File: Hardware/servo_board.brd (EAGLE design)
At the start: 30.5 x 50.8 mm, 33 parts, among them U1 PCA9685, U2 PCA9306

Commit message: Add version info
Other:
- board text added: "v01"
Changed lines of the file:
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@@
 <dimension x1="29.28210625" y1="41.83789375" x2="27.86789375" y2="43.25210625" x3="34.29" y3="48.26" textsize="1.778" layer="51" dtype="diameter"/>
 <text x="29.21" y="6.35" size="1.016" layer="22" font="vector" ratio="15" rot="MR90" align="center">4xM2.0</text>
+<text x="1.27" y="3.81" size="1.778" layer="1" font="vector" ratio="15">v01</text>
 </plain>
 <attributes>
@@
 <wire x1="3.048" y1="40.005" x2="1.905" y2="40.005" width="0.254" layer="16"/>
 <via x="16.51" y="13.97" extent="1-16" drill="0.508"/>
-<wire x1="27.1272" y1="20.5232" x2="28.2448" y2="22.1742" width="0" layer="19" extent="1-1"/>
-<wire x1="25.96" y1="20.58" x2="27.1272" y2="20.5232" width="0" layer="19" extent="16-16"/>
-<wire x1="25.96" y1="20.5798" x2="25.96" y2="20.58" width="0" layer="19" extent="1-16"/>
-<wire x1="25.96" y1="20.98" x2="25.96" y2="20.58" width="0" layer="19" extent="16-16"/>
-<wire x1="25.96" y1="20.9798" x2="25.96" y2="20.98" width="0" layer="19" extent="1-16"/>
-<wire x1="25.96" y1="21.38" x2="25.96" y2="20.98" width="0" layer="19" extent="16-16"/>
-<wire x1="25.96" y1="21.3798" x2="25.96" y2="21.38" width="0" layer="19" extent="1-16"/>
-<wire x1="25.96" y1="20.18" x2="25.96" y2="20.58" width="0" layer="19" extent="16-16"/>
-<wire x1="25.96" y1="20.1798" x2="25.96" y2="20.18" width="0" layer="19" extent="1-16"/>
-<wire x1="25.96" y1="22.18" x2="25.96" y2="21.38" width="0" layer="19" extent="16-16"/>
-<wire x1="25.96" y1="22.1798" x2="25.96" y2="22.18" width="0" layer="19" extent="1-16"/>
-<wire x1="25.96" y1="22.98" x2="25.96" y2="22.18" width="0" layer="19" extent="16-16"/>
-<wire x1="25.96" y1="22.9798" x2="25.96" y2="22.98" width="0" layer="19" extent="1-16"/>
-<wire x1="17.145" y1="26.25" x2="25.96" y2="22.98" width="0" layer="19" extent="1-16"/>
-<wire x1="13.705" y1="28.6" x2="17.145" y2="26.25" width="0" layer="19" extent="1-1"/>
-<wire x1="13.055" y1="28.6" x2="13.705" y2="28.6" width="0" layer="19" extent="1-1"/>
-<wire x1="13.705" y1="22.2" x2="17.145" y2="26.25" width="0" layer="19" extent="1-1"/>
-<wire x1="13.055" y1="22.2" x2="13.705" y2="22.2" width="0" layer="19" extent="1-1"/>
-<wire x1="12.405" y1="22.2" x2="13.055" y2="22.2" width="0" layer="19" extent="1-1"/>
-<wire x1="7.205" y1="28.6" x2="13.055" y2="28.6" width="0" layer="19" extent="1-1"/>
-<wire x1="8.04" y1="15.24" x2="12.405" y2="22.2" width="0" layer="19" extent="1-1"/>
-<wire x1="10.199" y1="11.43" x2="8.04" y2="15.24" width="0" layer="19" extent="1-1"/>
-<wire x1="14.74" y1="12.5238" x2="10.199" y2="11.43" width="0" layer="19" extent="1-1"/>
-<wire x1="16.51" y1="13.97" x2="14.74" y2="12.5238" width="0" layer="19" extent="1-1"/>
-<wire x1="3.048" y1="40.005" x2="7.205" y2="28.6" width="0" layer="19" extent="1-16"/>
 </signal>
 <signal name="VSYS">

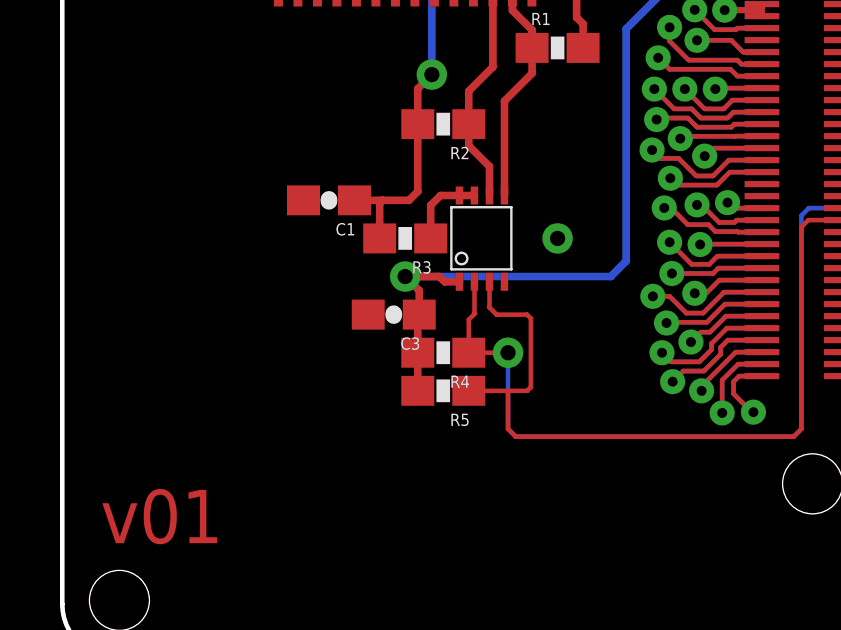
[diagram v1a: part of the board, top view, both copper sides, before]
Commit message: Touch up silk, resistor placement
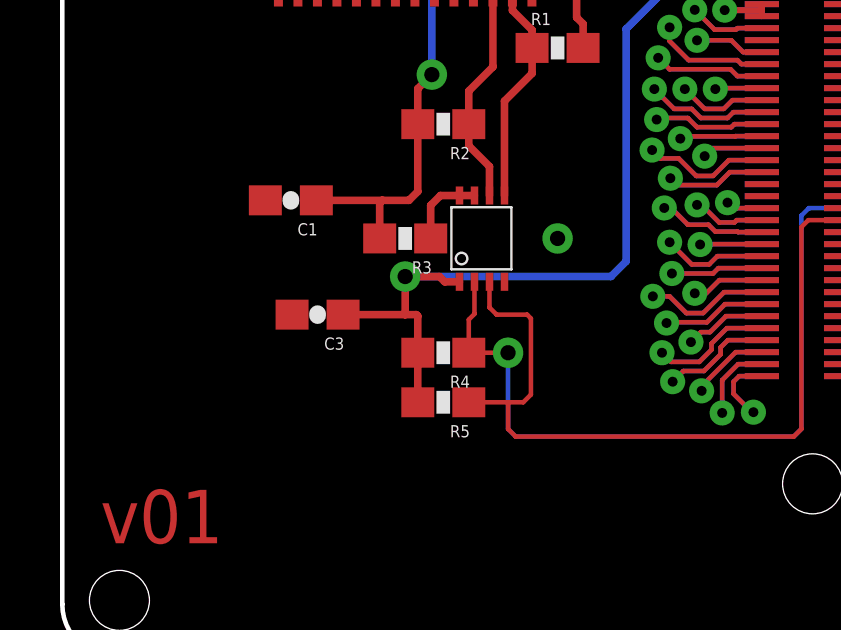
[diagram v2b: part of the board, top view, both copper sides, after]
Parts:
- moved C3 2.54 mm to (8.51, 11.4)
- moved C1 1.27 mm to (7.62, 15.2)
- moved R5 0.38 mm to (12.7, 8.51)
- renumbered U$2 to U3, U$3 to U4
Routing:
- net 1.8V: track 29.4 -> 32.0 mm
- net VSYS: track 32.5 -> 33.7 mm
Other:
- board text added: "8-Servo Controller"
- board text added: "GND"
- board text added: "M Hord"
- board text added: "SIG"
- board text added: "VIN"
- board text removed: "Casey Kuhns"
- board text removed: "Example Name of Board"

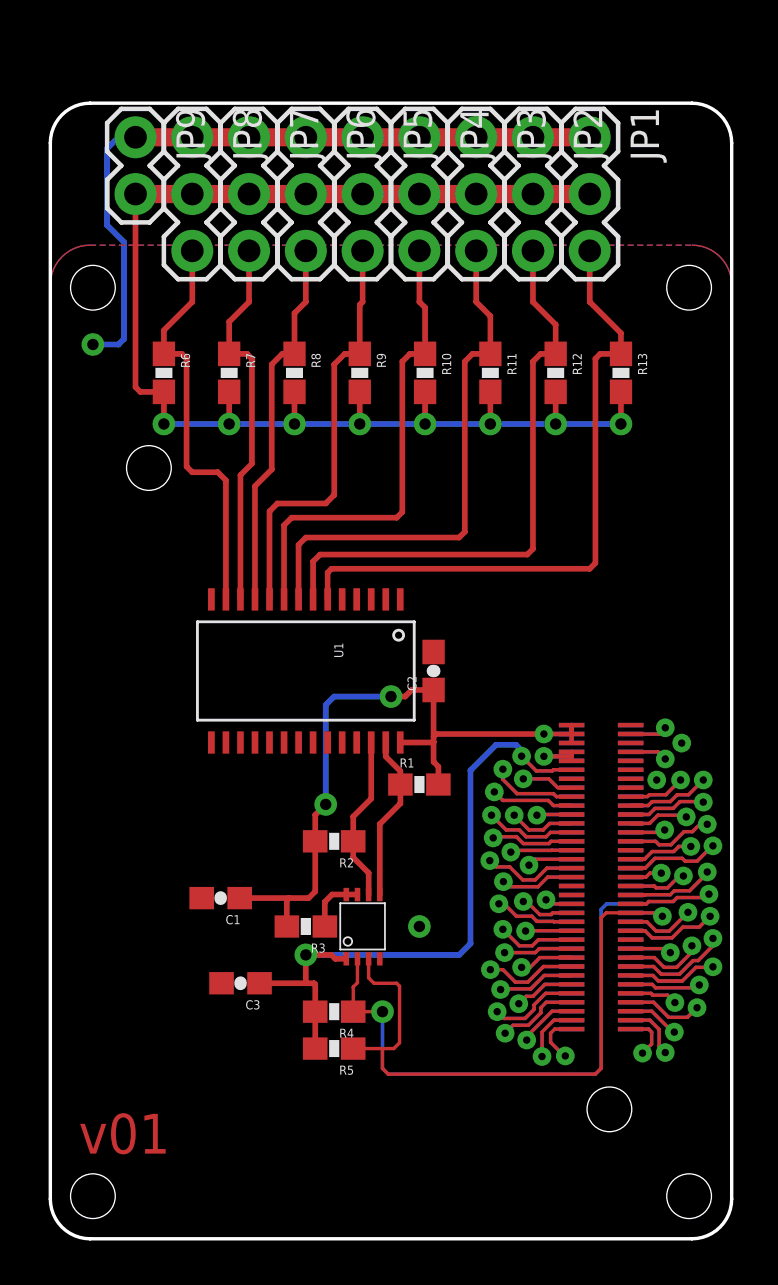
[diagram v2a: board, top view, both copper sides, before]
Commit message: Increased length of board by 100th
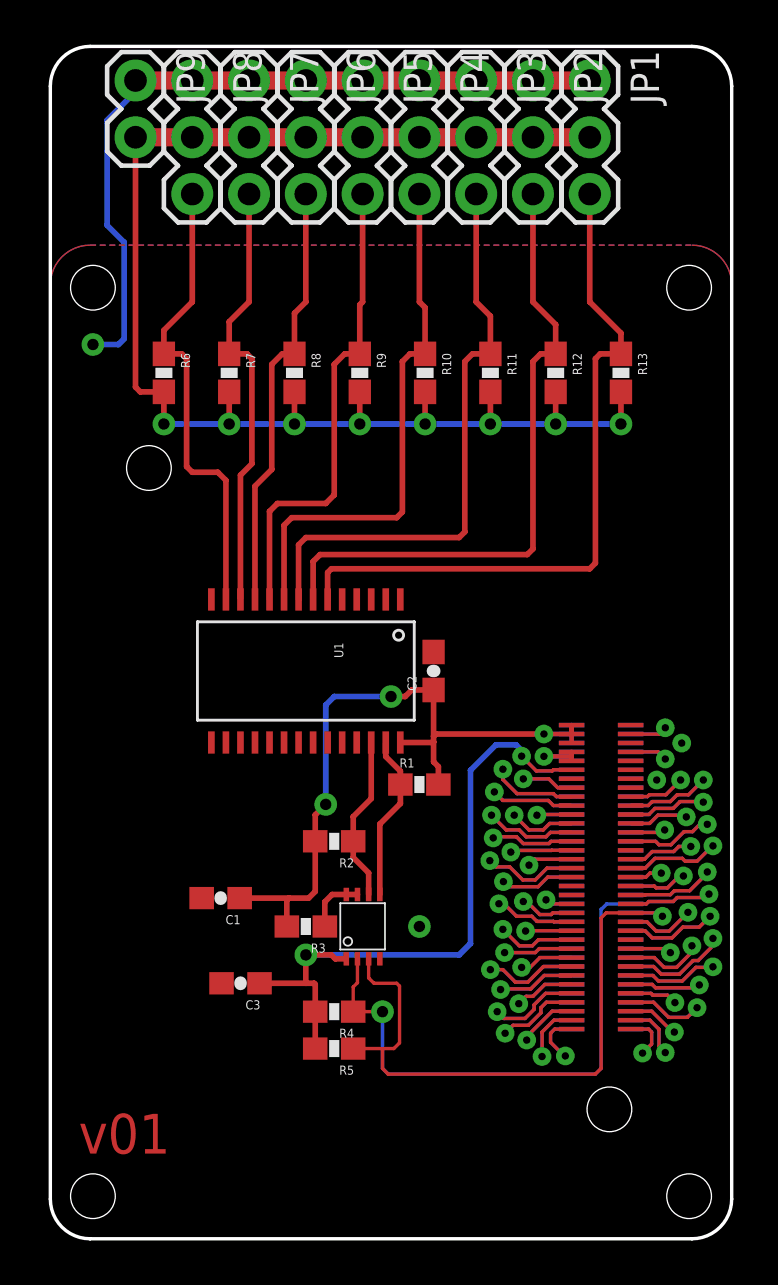
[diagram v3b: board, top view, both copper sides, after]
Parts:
- moved JP1 2.54 mm to (24.1, 51.8)
- moved JP2 2.54 mm to (21.6, 51.8)
- moved JP3 2.54 mm to (19.1, 51.8)
- moved JP4 2.54 mm to (16.5, 51.8)
- moved JP5 2.54 mm to (14.0, 51.8)
- moved JP6 2.54 mm to (11.4, 51.8)
- moved JP7 2.54 mm to (8.89, 51.8)
- moved JP8 2.54 mm to (6.35, 51.8)
- moved JP9 2.54 mm to (3.81, 51.8)
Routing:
- net VCC: track 62.3 -> 64.8 mm
- net CH5: track 16.9 -> 19.4 mm
- net CH2: track 23.9 -> 26.4 mm
- net CH1: track 26.3 -> 28.9 mm
- net CH7: track 18.4 -> 21.0 mm
- net CH6: track 17.1 -> 19.6 mm
- net CH4: track 19.0 -> 21.5 mm
- net CH3: track 21.5 -> 24.0 mm
- net CH0: track 28.9 -> 31.5 mm
- net GND: track 32.1 -> 34.2 mm
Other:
- board size 30.5 x 50.8 mm -> 30.5 x 53.3 mm

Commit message: Skootch resistors out of keepout region.
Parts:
- moved R12 3.81 mm to (22.6, 42.5)
- moved R13 3.81 mm to (25.5, 42.5)
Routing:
- net VCC: track 64.8 -> 68.0 mm
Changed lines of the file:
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@@
 <attribute name="PROD_ID" value="RES-07856" x="0.635" y="56.515" size="1.778" layer="27" font="vector" ratio="15" rot="R270" display="off"/>
 </element>
-<element name="R12" library="SparkFun-Resistors" package="0603-RES" value="1K" x="22.606" y="38.735" rot="R270">
-<attribute name="PROD_ID" value="RES-07856" x="-0.254" y="60.325" size="1.778" layer="27" font="vector" ratio="15" rot="R270" display="off"/>
+<element name="R12" library="SparkFun-Resistors" package="0603-RES" value="1K" x="22.606" y="42.545" rot="R270">
+<attribute name="PROD_ID" value="RES-07856" x="-0.254" y="64.135" size="1.778" layer="27" font="vector" ratio="15" rot="R270" display="off"/>
 </element>
-<element name="R13" library="SparkFun-Resistors" package="0603-RES" value="1K" x="25.527" y="38.735" rot="R270">
-<attribute name="PROD_ID" value="RES-07856" x="-1.143" y="64.135" size="1.778" layer="27" font="vector" ratio="15" rot="R270" display="off"/>
+<element name="R13" library="SparkFun-Resistors" package="0603-RES" value="1K" x="25.527" y="42.545" rot="R270">
+<attribute name="PROD_ID" value="RES-07856" x="-1.143" y="67.945" size="1.778" layer="27" font="vector" ratio="15" rot="R270" display="off"/>
 </element>
 <element name="JP1" library="SparkFun-Connectors" package="1X03" value="" x="24.13" y="51.816" rot="R270"/>
@@
 <contactref element="U1" pad="6"/>
 <contactref element="JP1" pad="3"/>
-<wire x1="25.527" y1="39.585" x2="25.527" y2="40.513" width="0.254" layer="1"/>
-<wire x1="25.527" y1="40.513" x2="24.13" y2="41.91" width="0.254" layer="1"/>
-<wire x1="24.13" y1="41.91" x2="24.13" y2="46.736" width="0.254" layer="1"/>
+<wire x1="25.527" y1="43.395" x2="25.527" y2="44.323" width="0.254" layer="1"/>
+<wire x1="25.527" y1="44.323" x2="24.13" y2="45.72" width="0.254" layer="1"/>
+<wire x1="24.13" y1="45.72" x2="24.13" y2="46.736" width="0.254" layer="1"/>
 <wire x1="12.405" y1="28.6" x2="12.405" y2="29.804" width="0.254" layer="1"/>
 <wire x1="12.405" y1="29.804" x2="12.573" y2="29.972" width="0.254" layer="1"/>
-<wire x1="12.573" y1="29.972" x2="24.13" y2="29.972" width="0.254" layer="1"/>
-<wire x1="24.13" y1="29.972" x2="24.384" y2="30.226" width="0.254" layer="1"/>
-<wire x1="24.384" y1="30.226" x2="24.384" y2="39.37" width="0.254" layer="1"/>
-<wire x1="24.384" y1="39.37" x2="24.599" y2="39.585" width="0.254" layer="1"/>
-<wire x1="25.527" y1="39.585" x2="24.599" y2="39.585" width="0.254" layer="1"/>
+<wire x1="12.573" y1="29.972" x2="21.336" y2="29.972" width="0.254" layer="1"/>
+<wire x1="21.336" y1="29.972" x2="21.59" y2="30.226" width="0.254" layer="1"/>
+<wire x1="21.59" y1="30.226" x2="21.59" y2="39.37" width="0.254" layer="1"/>
+<wire x1="21.59" y1="39.37" x2="21.717" y2="39.497" width="0.254" layer="1"/>
+<wire x1="21.717" y1="39.497" x2="24.003" y2="39.497" width="0.254" layer="1"/>
+<wire x1="24.003" y1="39.497" x2="24.384" y2="39.878" width="0.254" layer="1"/>
+<wire x1="24.384" y1="39.878" x2="24.384" y2="43.18" width="0.254" layer="1"/>
+<wire x1="24.384" y1="43.18" x2="24.599" y2="43.395" width="0.254" layer="1"/>
+<wire x1="25.527" y1="43.395" x2="24.599" y2="43.395" width="0.254" layer="1"/>
 </signal>
 <signal name="CH1">
@@
 <contactref element="U1" pad="7"/>
 <contactref element="JP2" pad="3"/>
-<wire x1="22.606" y1="39.585" x2="22.606" y2="40.894" width="0.254" layer="1"/>
-<wire x1="22.606" y1="40.894" x2="21.59" y2="41.91" width="0.254" layer="1"/>
-<wire x1="21.59" y1="41.91" x2="21.59" y2="46.736" width="0.254" layer="1"/>
+<wire x1="22.606" y1="43.395" x2="22.606" y2="44.704" width="0.254" layer="1"/>
+<wire x1="22.606" y1="44.704" x2="21.59" y2="45.72" width="0.254" layer="1"/>
+<wire x1="21.59" y1="45.72" x2="21.59" y2="46.736" width="0.254" layer="1"/>
 <wire x1="11.755" y1="28.6" x2="11.755" y2="30.297" width="0.254" layer="1"/>
 <wire x1="11.755" y1="30.297" x2="12.065" y2="30.607" width="0.254" layer="1"/>
-<wire x1="12.065" y1="30.607" x2="21.336" y2="30.607" width="0.254" layer="1"/>
-<wire x1="21.336" y1="30.607" x2="21.59" y2="30.861" width="0.254" layer="1"/>
-<wire x1="21.59" y1="30.861" x2="21.59" y2="39.243" width="0.254" layer="1"/>
-<wire x1="22.606" y1="39.585" x2="21.932" y2="39.585" width="0.254" layer="1"/>
-<wire x1="21.932" y1="39.585" x2="21.59" y2="39.243" width="0.254" layer="1"/>
+<wire x1="12.065" y1="30.607" x2="20.32" y2="30.607" width="0.254" layer="1"/>
+<wire x1="20.32" y1="30.607" x2="20.701" y2="30.988" width="0.254" layer="1"/>
+<wire x1="20.701" y1="30.988" x2="20.701" y2="42.545" width="0.254" layer="1"/>
+<wire x1="22.606" y1="43.395" x2="21.551" y2="43.395" width="0.254" layer="1"/>
+<wire x1="21.551" y1="43.395" x2="20.701" y2="42.545" width="0.254" layer="1"/>
 </signal>
 <signal name="CH2">
@@
 <wire x1="19.685" y1="37.885" x2="19.685" y2="36.449" width="0.254" layer="1"/>
 <via x="19.685" y="36.449" extent="1-16" drill="0.508"/>
-<wire x1="22.606" y1="37.885" x2="22.606" y2="36.449" width="0.254" layer="1"/>
-<via x="22.606" y="36.449" extent="1-16" drill="0.508"/>
-<wire x1="25.527" y1="37.885" x2="25.527" y2="36.449" width="0.254" layer="1"/>
-<via x="25.527" y="36.449" extent="1-16" drill="0.508"/>
-<wire x1="25.527" y1="36.449" x2="22.606" y2="36.449" width="0.254" layer="16"/>
-<wire x1="19.685" y1="36.449" x2="22.606" y2="36.449" width="0.254" layer="16"/>
+<wire x1="22.606" y1="41.695" x2="22.606" y2="40.386" width="0.254" layer="1"/>
+<via x="22.606" y="40.386" extent="1-16" drill="0.508"/>
+<wire x1="25.527" y1="41.695" x2="25.527" y2="40.386" width="0.254" layer="1"/>
+<via x="25.527" y="40.386" extent="1-16" drill="0.508"/>
+<wire x1="25.527" y1="40.386" x2="22.606" y2="40.386" width="0.254" layer="16"/>
+<wire x1="19.685" y1="36.449" x2="20.574" y2="36.449" width="0.254" layer="16"/>
+<wire x1="20.574" y1="36.449" x2="20.955" y2="36.83" width="0.254" layer="16"/>
+<wire x1="20.955" y1="36.83" x2="20.955" y2="39.878" width="0.254" layer="16"/>
+<wire x1="20.955" y1="39.878" x2="21.463" y2="40.386" width="0.254" layer="16"/>
+<wire x1="21.463" y1="40.386" x2="22.606" y2="40.386" width="0.254" layer="16"/>
 <wire x1="19.685" y1="36.449" x2="16.764" y2="36.449" width="0.254" layer="16"/>
 <wire x1="16.764" y1="36.449" x2="13.843" y2="36.449" width="0.254" layer="16"/>

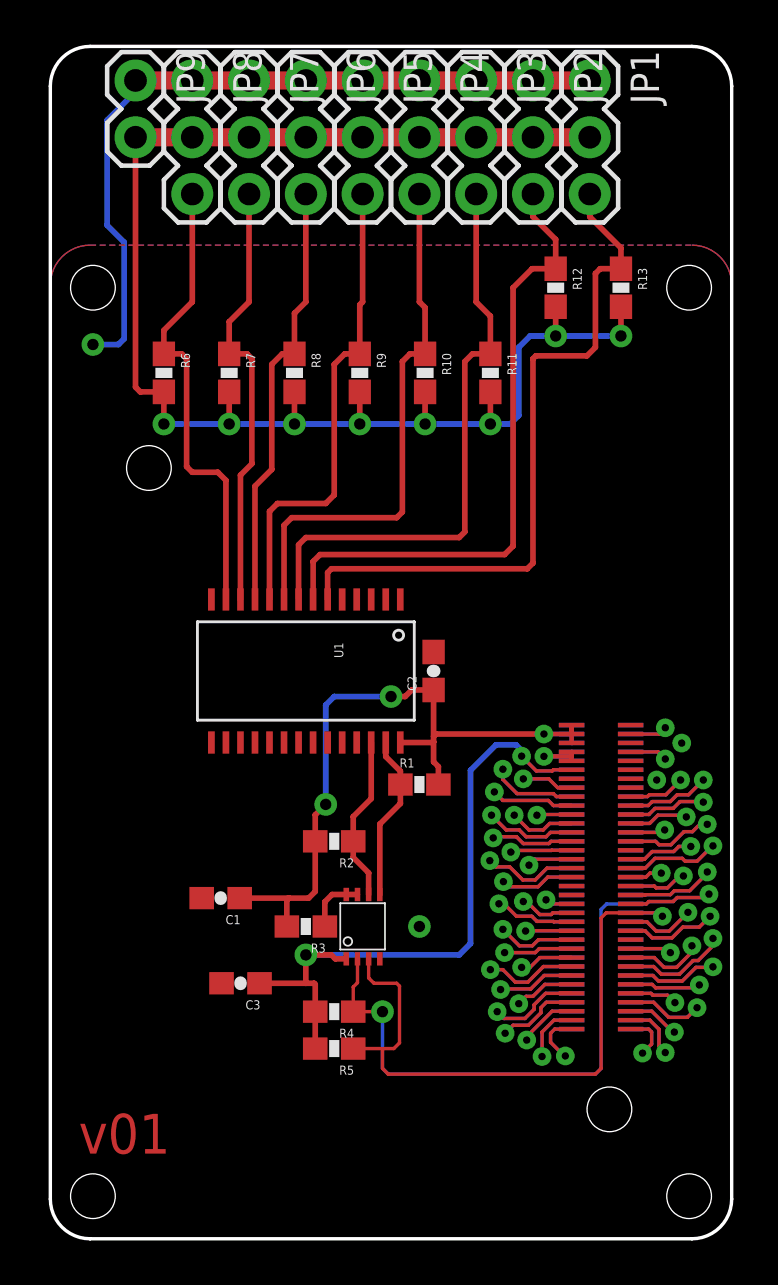
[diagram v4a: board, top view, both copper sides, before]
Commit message: Move resistors and traces out of restrict zone
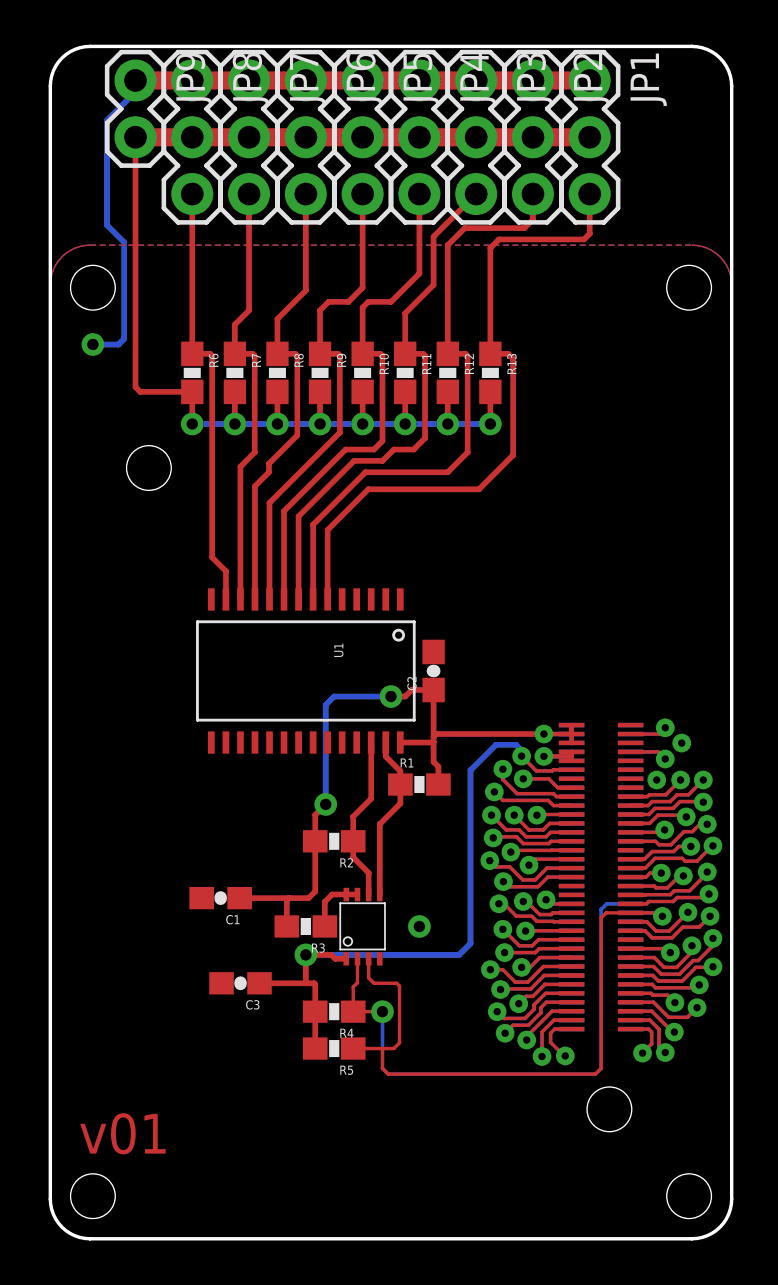
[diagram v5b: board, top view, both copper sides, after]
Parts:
- moved R13 6.97 mm to (19.7, 38.7)
- moved R12 6.15 mm to (17.8, 38.7)
- moved R11 3.81 mm to (15.9, 38.7)
- moved R10 2.79 mm to (14.0, 38.7)
- moved R9 1.78 mm to (12.1, 38.7)
- moved R6 1.27 mm to (6.35, 38.7)
- moved R8 0.76 mm to (10.2, 38.7)
- moved R7 0.25 mm to (8.26, 38.7)
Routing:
- net VCC: track 68.0 -> 58.9 mm
- net CH2: track 26.4 -> 23.9 mm
- net CH0: track 31.2 -> 29.4 mm
- net CH7: track 21.0 -> 19.2 mm
- net CH1: track 28.5 -> 27.1 mm
- net CH5: track 19.4 -> 20.3 mm
- net CH3: track 24.0 -> 23.2 mm
